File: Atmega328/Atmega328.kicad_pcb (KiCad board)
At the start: 2 copper layers, 48.3 x 66 mm, 30 parts, among them J1 Conn_01x02, J2 Conn_02x03_Odd_Even, J3 Conn_01x14, SW1 SW_Push, U1 LM358, U2 LM358, U3 LM78M05_TO252, U4 ATmega328P-PU, U5 DHT11, Y1 12MHz

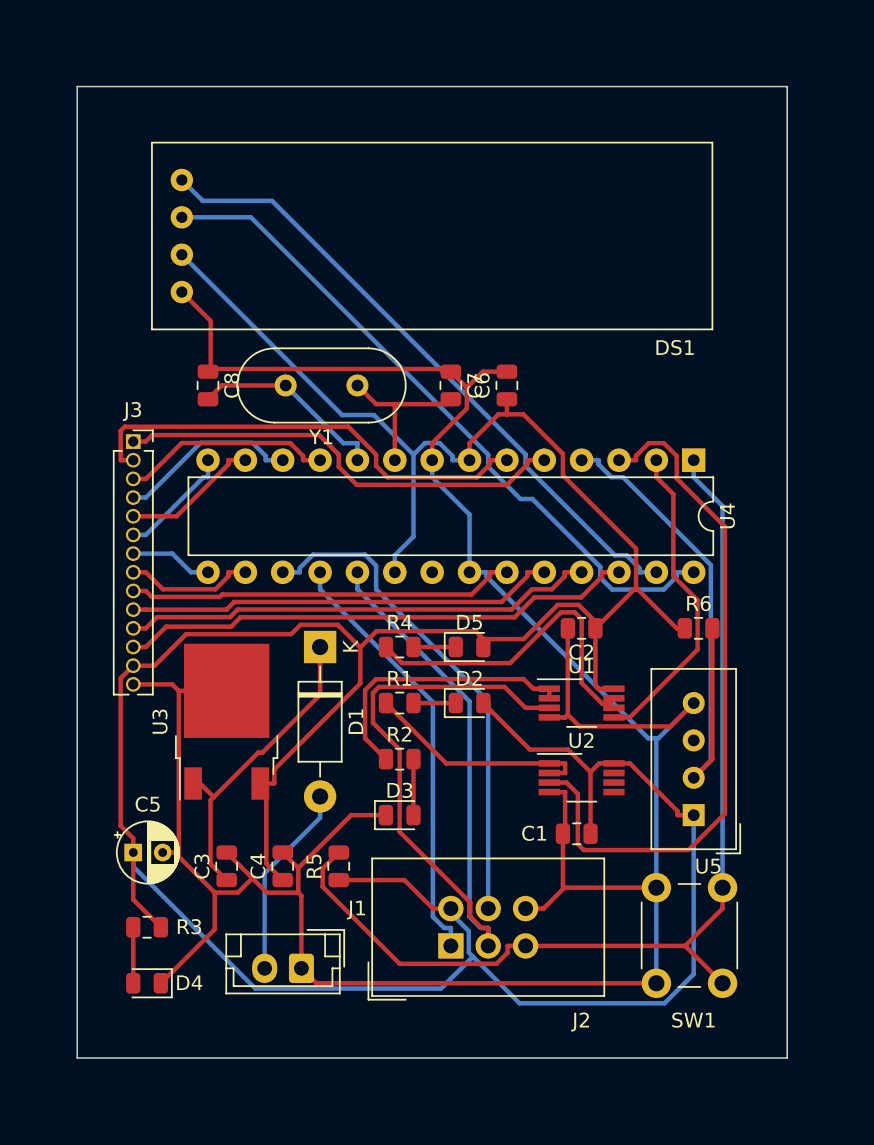
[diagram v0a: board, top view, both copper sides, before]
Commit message: Add Ground Zone on the back
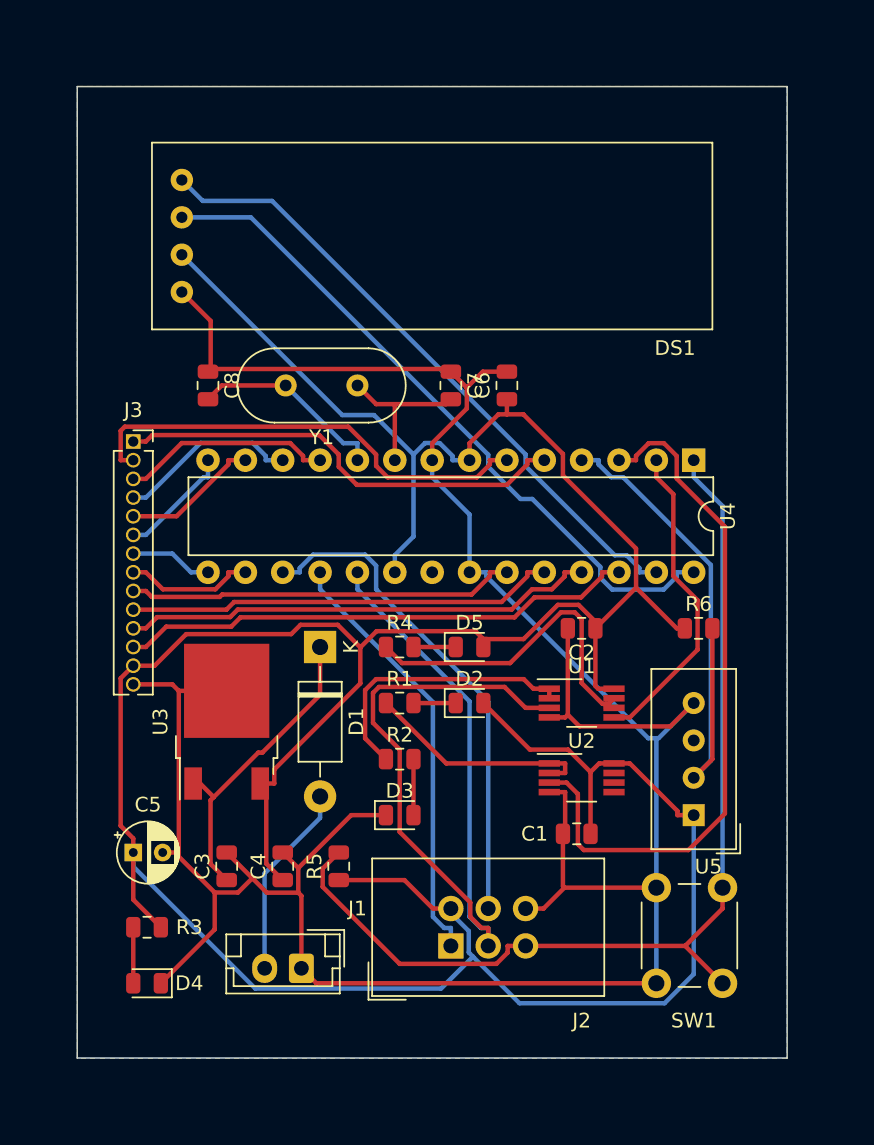
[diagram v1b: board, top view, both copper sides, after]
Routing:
- added copper zone on B.Cu, net GND

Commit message: Fix footprints
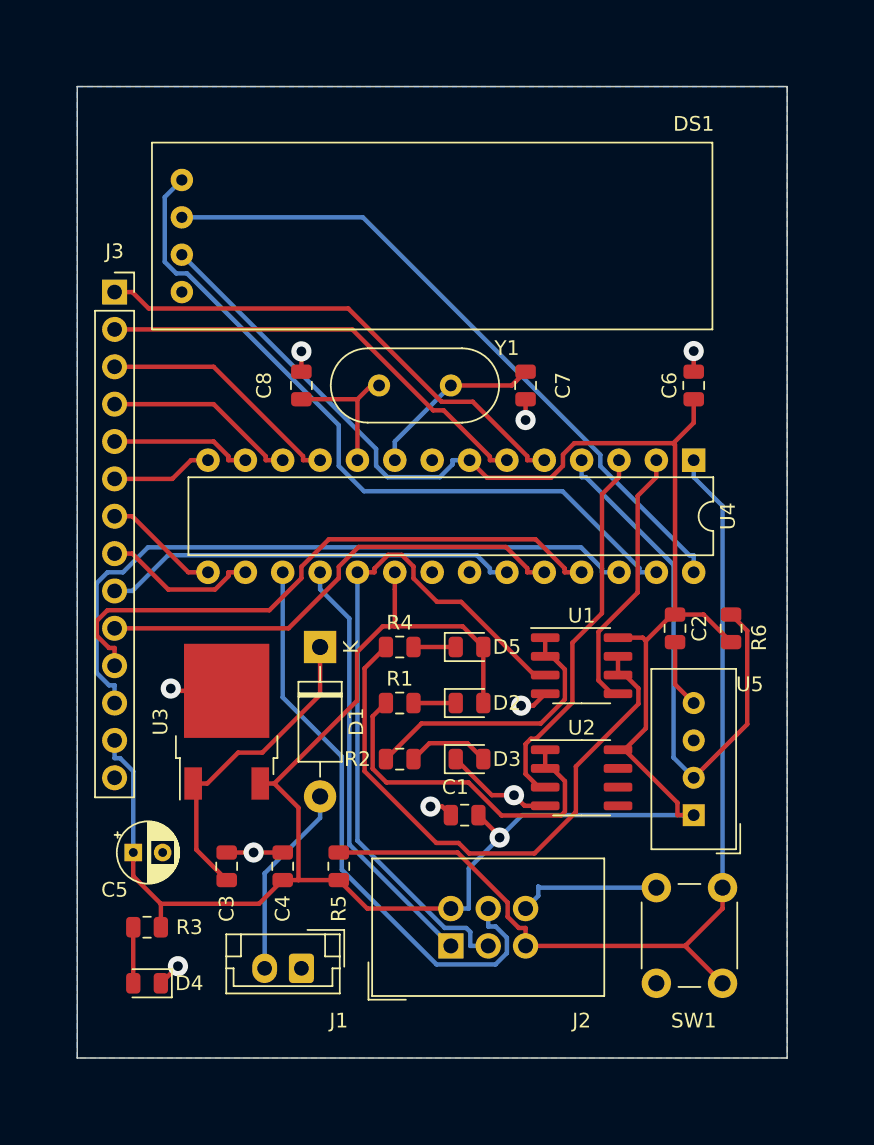
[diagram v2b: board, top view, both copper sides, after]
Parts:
- J3: footprint Connector_PinSocket_1.27mm:PinSocket_1x14_P1.27mm_Vertical -> Connector_PinSocket_2.54mm:PinSocket_1x14_P2.54mm_Vertical
- U1, U2: footprint Package_SO:VSSOP-8_3.0x3.0mm_P0.65mm -> Package_SO:SOIC-8_3.9x4.9mm_P1.27mm
- moved C6 12.7 mm to (124.5, 45.7)
- moved J3 10.2 mm to (85.1, 39.4)
- moved C1 7.73 mm to (108.9, 74.9)
- moved C8 6.35 mm to (97.8, 45.7)
- moved Y1 6.35 mm to (108.0, 45.7)
- moved C2 6.35 mm to (123.2, 62.2), turned to 270 degrees
- moved D3 6.09 mm to (109.2, 71.1)
- moved C7 5.08 mm to (113.0, 45.7), turned to 90 degrees
- moved U1 2.54 mm to (116.8, 64.8)
- moved R6 2.21 mm to (127.0, 62.2), turned to 90 degrees
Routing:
- net GND: track 193.0 -> 39.1 mm, vias 0 -> 9
- net +5V: track 236.1 -> 178.1 mm, vias 0 -> 1
- net /TXLED: track 47.5 -> 25.9 mm
- net Net-(R4-Pad1): track 23.5 -> 40.1 mm
- net /SCK: track 62.8 -> 47.9 mm
- net /ARD_17: track 35.3 -> 46.3 mm
- net Net-(R1-Pad1): track 15.6 -> 24.4 mm
- net /ARD_16: track 32.2 -> 40.6 mm
- net /MOSI: track 33.8 -> 39.9 mm
- net /SDA: track 43.9 -> 50.0 mm
- net /ARD_15: track 29.2 -> 32.8 mm
- net /XTAL2: track 13.3 -> 9.81 mm
- net /RXLED: track 21.6 -> 18.3 mm
- net /ARD_3: track 30.9 -> 34.1 mm
- net /RESET: track 68.8 -> 65.9 mm
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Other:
- net class Power added: clearance 0.254, trace_width 0.508, via_dia 2.032, via_drill 0.889

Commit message: PCB Cleanup and Ready
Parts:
- added M1: MountingHole_2.5mm_Pad, MountingHole:MountingHole_2.5mm_Pad, F.Cu at (84.5, 26.7)
- added M2: MountingHole_2.5mm_Pad, MountingHole:MountingHole_2.5mm_Pad, F.Cu at (129.5, 26.7)
- added M3: MountingHole_2.5mm_Pad, MountingHole:MountingHole_2.5mm_Pad, F.Cu at (129.5, 90.8)
- added M4: MountingHole_2.5mm_Pad, MountingHole:MountingHole_2.5mm_Pad, F.Cu at (84.5, 90.8)
- D1: footprint Diode_THT:D_DO-41_SOD81_P10.16mm_Horizontal -> Diode_THT:D_DO-34_SOD68_P7.62mm_Horizontal
- moved J1 2.55 mm to (95.2, 85.1), turned to 0 degrees
- moved C5 1.27 mm to (87.6, 77.5), turned to 270 degrees
- moved U3 0.90 mm to (92.1, 67.9)
- moved D1 0.64 mm to (98.4, 63.5)
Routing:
- net GND: track 39.1 -> 272.6 mm, vias 9 -> 0
- net +5V: track 178.1 -> 248.8 mm, vias 1 -> 0
- net /MISO: track 29.1 -> 56.4 mm
- net /MOSI: track 39.9 -> 61.8 mm
- net Net-(R4-Pad1): track 40.1 -> 22.0 mm, vias 0 -> 2
- net /RESET: track 65.9 -> 81.7 mm
- net Net-(R1-Pad1): track 24.4 -> 14.8 mm, vias 0 -> 2
- net /ARD_17: track 46.3 -> 38.1 mm
- net /ARD_16: track 40.6 -> 34.5 mm
- net /SCK: track 47.9 -> 41.9 mm
- net /ARD_2: track 38.0 -> 32.0 mm
- net Net-(R2-Pad1): track 18.9 -> 15.6 mm
- net /SDA: track 50.0 -> 48.0 mm
- net /ARD_15: track 32.8 -> 30.9 mm
- net /RXLED: track 18.3 -> 20.1 mm
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- added copper zone on F.Cu, net GND
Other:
- board size 48.3 x 66 mm -> 55.2 x 73.7 mm
- board text added: "+"
- board text added: "+5V"
- board text added: "-"
- board text added: "1"
- board text added: "10"
- board text added: "14"
- board text added: "15"
- board text added: "16"
- board text added: "17"
- board text added: "3"
- board text added: "4"
- board text added: "5"
- board text added: "5V, MOSI, GND MISO, SCK, RST"
- board text added: "6"
- board text added: "7"
- board text added: "7+V DC in"
- board text added: "7805"
- board text added: "8"
- board text added: "9"
- board text added: "Arduino Pins"
- board text added: "Atmega Proto Board v1"
- board text added: "Atmega328P"
- board text added: "DHT11"
- board text added: "GND"
- board text added: "ICSP"
- board text added: "PWR"
- board text added: "Pratap Karonde"
- board text added: "RESET"
- board text added: "RX"
- board text added: "SCK"
- board text added: "SSD1306"
- board text added: "TX"
